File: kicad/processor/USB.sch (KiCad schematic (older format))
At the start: 18 parts, among them Q501 MMBT4401, Q502 MMBT4401, SW501 SWITCH_PUSHBUTTON, SW502 SWITCH_PUSHBUTTON, U501 USB_B_Socket, U502 SP3003-04, U503 CP2102N

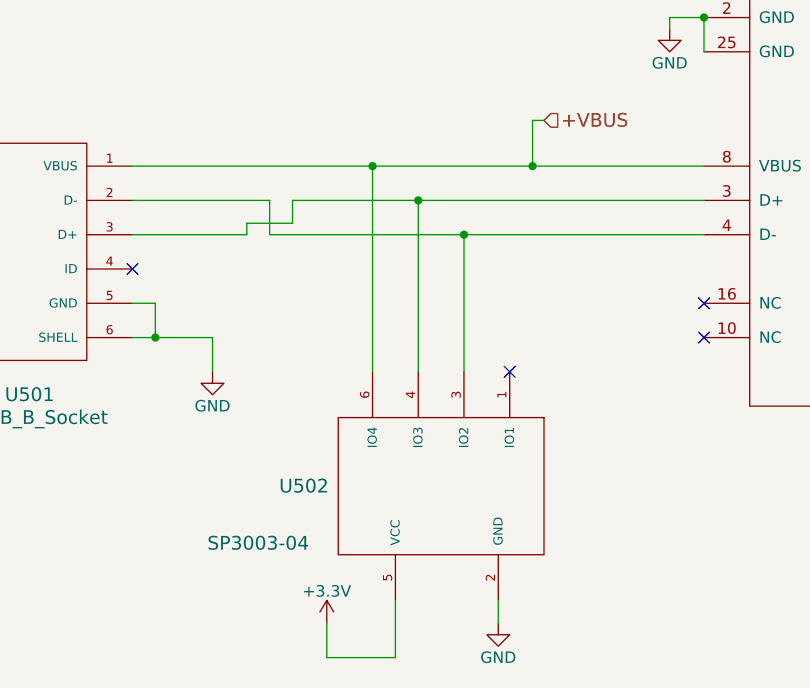
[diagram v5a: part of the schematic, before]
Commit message: Processor board routed, conn_FCI_14 switched to no hole version, port expander package fixed
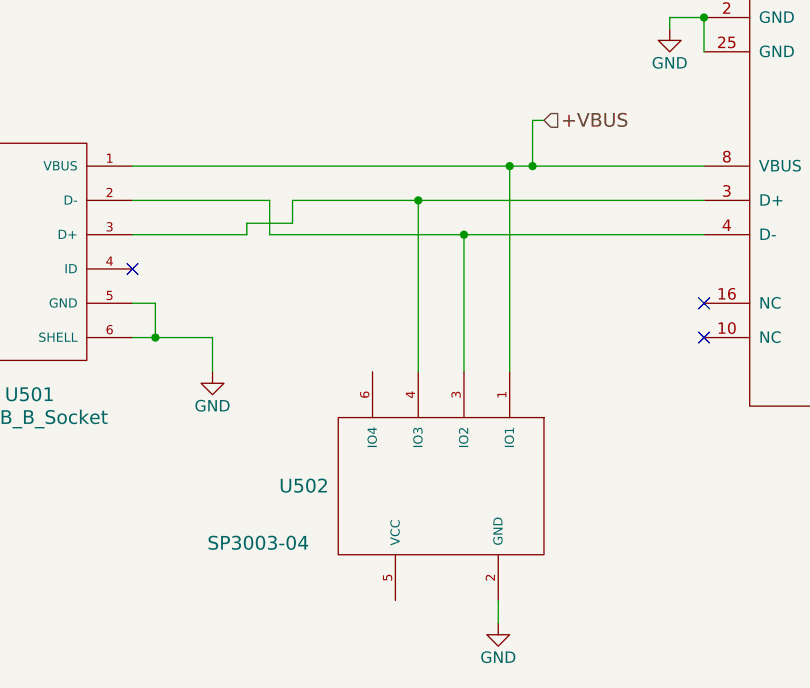
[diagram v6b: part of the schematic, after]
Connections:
- net +3V3: no longer U502.5 (VCC)
- net +VBUS: now also U502.1 (IO1); no longer U502.6 (IO4)
- no-connect marks 12 -> 11
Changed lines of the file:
@@
 	0    1    1    0
 $EndComp
-NoConn ~ 3800 4350
-$Comp
-L +3.3V #PWR072
-U 1 1 59CE83A8
-P 3000 5450
-F 0 "#PWR072" H 3000 5300 50  0001 C CNN
-F 1 "+3.3V" H 3000 5590 50  0000 C CNN
-F 2 "" H 3000 5450 50  0001 C CNN
-F 3 "" H 3000 5450 50  0001 C CNN
-	1    3000 5450
-	1    0    0    -1
-$EndComp
-$Comp
-L GND #PWR073
+$Comp
+L GND #PWR072
 U 1 1 59CE8429
 P 3750 5450
-F 0 "#PWR073" H 3750 5200 50  0001 C CNN
+F 0 "#PWR072" H 3750 5200 50  0001 C CNN
 F 1 "GND" H 3750 5300 50  0000 C CNN
 F 2 "" H 3750 5450 50  0001 C CNN
@@
 Connection ~ 3900 3450
 Wire Wire Line
-	3200 4350 3200 3450
-Connection ~ 3200 3450
-Wire Wire Line
 	3600 4350 3600 3750
 Connection ~ 3600 3750
 Wire Wire Line
-	3300 5350 3300 5600
-Wire Wire Line
-	3300 5600 3000 5600
-Wire Wire Line
-	3000 5600 3000 5450
-Wire Wire Line
 	3750 5350 3750 5450
 Wire Wire Line
@@
 	9200 4900 9200 5000
 $Comp
-L GND #PWR074
+L GND #PWR073
 U 1 1 59CC74B7
 P 9200 5000
-F 0 "#PWR074" H 9200 4750 50  0001 C CNN
+F 0 "#PWR073" H 9200 4750 50  0001 C CNN
 F 1 "GND" H 9200 4850 50  0000 C CNN
 F 2 "" H 9200 5000 50  0001 C CNN
@@
 $EndComp
 $Comp
-L GND #PWR075
+L GND #PWR074
 U 1 1 59CC74F8
 P 9150 3400
-F 0 "#PWR075" H 9150 3150 50  0001 C CNN
+F 0 "#PWR074" H 9150 3150 50  0001 C CNN
 F 1 "GND" H 9150 3250 50  0000 C CNN
 F 2 "" H 9150 3400 50  0001 C CNN
@@
 Wire Wire Line
 	9000 4050 6150 4050
+Wire Wire Line
+	3800 4350 3800 3450
+Connection ~ 3800 3450
 $EndSCHEMATC

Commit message: processor RC1
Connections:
- no-connect marks 11 -> 13
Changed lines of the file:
@@
 	3800 4350 3800 3450
 Connection ~ 3800 3450
+NoConn ~ 3200 4350
+NoConn ~ 3300 5350
 $EndSCHEMATC

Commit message: Switch to nightly Windows build
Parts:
- C501, C502: symbol C_Small -> device:C_Small
- LED501, LED502: symbol LED -> device:LED
- Q501, Q502: symbol NPN_BEC_SOT-23 -> paddle:NPN_BEC_SOT-23
- R501, R502, R503, R504, R505: symbol R_US -> paddle:R_US
- SW501, SW502: symbol SWITCH_PUSHBUTTON -> paddle:SWITCH_PUSHBUTTON
- TP501, TP502: symbol TEST -> processor-rescue:TEST-RESCUE-processor
- U501: symbol USB_B_Socket -> paddle:USB_B_Socket
- U502: symbol SP3003-04 -> paddle:SP3003-04
- U503: symbol CP2104 -> paddle:CP2104
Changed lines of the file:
@@
-EESchema Schematic File Version 2
-LIBS:power
-LIBS:device
-LIBS:transistors
-LIBS:conn
-LIBS:linear
-LIBS:regul
-LIBS:paddle
+EESchema Schematic File Version 4
 LIBS:processor-cache
-EELAYER 25 0
+EELAYER 26 0
 EELAYER END
 $Descr A4 11693 8268
@@
 $EndDescr
 $Comp
-L CP2104 U503
+L paddle:CP2104 U503
 U 1 1 59C7A894
 P 5400 3300
@@
 $EndComp
 $Comp
-L GND #PWR064
+L power:GND #PWR064
 U 1 1 59C7A89B
 P 4500 2850
@@
 $EndComp
 $Comp
-L C_Small C502
+L device:C_Small C502
 U 1 1 59C7A8A4
 P 4400 2350
@@
 $EndComp
 $Comp
-L GND #PWR065
+L power:GND #PWR065
 U 1 1 59C7A8AB
 P 4400 2500
@@
 $EndComp
 $Comp
-L C_Small C501
+L device:C_Small C501
 U 1 1 59C7A8B1
 P 4150 2350
@@
 $EndComp
 $Comp
-L GND #PWR066
+L power:GND #PWR066
 U 1 1 59C7A8B8
 P 4150 2500
@@
 NoConn ~ 4650 4200
 $Comp
-L NPN_BEC_SOT-23 Q501
+L paddle:NPN_BEC_SOT-23 Q501
 U 1 1 59C7A8C7
 P 7900 5150
@@
 $EndComp
 $Comp
-L NPN_BEC_SOT-23 Q502
+L paddle:NPN_BEC_SOT-23 Q502
 U 1 1 59C7A8CE
 P 7950 3600
@@
 $EndComp
 $Comp
-L R_US R505
+L paddle:R_US R505
 U 1 1 59C7A8D5
 P 7300 5150
@@
 $EndComp
 $Comp
-L R_US R504
+L paddle:R_US R504
 U 1 1 59C7A8DC
 P 7250 3600
@@
 +VBUS
 $Comp
-L LED LED502
+L device:LED LED502
 U 1 1 59C748D3
 P 7300 2950
@@
 $EndComp
 $Comp
-L R_US R503
+L paddle:R_US R503
 U 1 1 59C74976
 P 6800 2950
@@
 $EndComp
 $Comp
-L LED LED501
+L device:LED LED501
 U 1 1 59C74B26
 P 7300 2650
@@
 $EndComp
 $Comp
-L R_US R502
+L paddle:R_US R502
 U 1 1 59C74B2C
 P 6800 2650
@@
 $EndComp
 $Comp
-L GND #PWR067
+L power:GND #PWR067
 U 1 1 59C74BF4
 P 7650 2750
@@
 $EndComp
 $Comp
-L GND #PWR068
+L power:GND #PWR068
 U 1 1 59C74C20
 P 7600 3050
@@
 $EndComp
 $Comp
-L R_US R501
+L paddle:R_US R501
 U 1 1 59C74D40
 P 6500 2200
@@
 $EndComp
 $Comp
-L +3.3V #PWR069
+L power:+3.3V #PWR069
 U 1 1 59C74D81
 P 3900 2100
@@
 $EndComp
 $Comp
-L +3.3V #PWR070
+L power:+3.3V #PWR070
 U 1 1 59C74E3F
 P 6900 2100
@@
 $EndComp
 $Comp
-L GND #PWR071
+L power:GND #PWR071
 U 1 1 59CE40B1
 P 2500 4350
@@
 $EndComp
 $Comp
-L USB_B_Socket U501
+L paddle:USB_B_Socket U501
 U 1 1 59CE57D2
 P 1750 3800
@@
 NoConn ~ 2150 3900
 $Comp
-L SP3003-04 U502
+L paddle:SP3003-04 U502
 U 1 1 59CE7D75
 P 3500 4850
@@
 $EndComp
 $Comp
-L GND #PWR072
+L power:GND #PWR072
 U 1 1 59CE8429
 P 3750 5450
@@
 $EndComp
 $Comp
-L TEST TP502
+L processor-rescue:TEST-RESCUE-processor TP502
 U 1 1 59D07069
 P 9300 3900
+AR Path="/59D07069" Ref="TP502"  Part="1"
+AR Path="/59FFAD44/59D07069" Ref="TP502"  Part="1"
 F 0 "TP502" H 9300 4200 50  0000 C BNN
 F 1 "TXD" H 9300 4150 50  0000 C CNN
@@
 $EndComp
 $Comp
-L TEST TP501
+L processor-rescue:TEST-RESCUE-processor TP501
 U 1 1 59D07090
 P 9000 4050
+AR Path="/59D07090" Ref="TP501"  Part="1"
+AR Path="/59FFAD44/59D07090" Ref="TP501"  Part="1"
 F 0 "TP501" H 9000 4350 50  0000 C BNN
 F 1 "RXD" H 9000 4300 50  0000 C CNN
@@
 	9200 4900 9200 5000
 $Comp
-L GND #PWR073
+L power:GND #PWR073
 U 1 1 59CC74B7
 P 9200 5000
@@
 $EndComp
 $Comp
-L GND #PWR074
+L power:GND #PWR074
 U 1 1 59CC74F8
 P 9150 3400
@@
 	2850 3600 4650 3600
 $Comp
-L SWITCH_PUSHBUTTON SW?
+L paddle:SWITCH_PUSHBUTTON SW?
 U 1 1 59D20095
 P 8800 3300
@@
 $EndComp
 $Comp
-L SWITCH_PUSHBUTTON SW?
+L paddle:SWITCH_PUSHBUTTON SW?
 U 1 1 59D200ED
 P 8850 4900
